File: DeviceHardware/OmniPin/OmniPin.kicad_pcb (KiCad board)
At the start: 2 copper layers, 32 x 38 mm, 52 parts, among them J1 USB_B_Micro, J2 2-1734839-4, J4 Conn_01x02_Pin, Q1 IRLML6402, Q2 IRLML6244, SW1 RST, SW2 BOOT, SW3 POWER, SW4 NEXT, U1 ESP32-C3-MINI-1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

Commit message: update pcb
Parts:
- moved J4 16.7 mm to (106.2, 100.6)
- moved SW2 14.0 mm to (109.5, 100.6)
- moved R5 2.05 mm to (121.5, 98.2), turned to 180 degrees
- moved D6 0.51 mm to (129.0, 97.2)
- moved R13 0.51 mm to (129.0, 98.7)
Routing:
- net GND: track 201.5 -> 214.7 mm, vias 6 -> 9
- net RX: track 6.41 -> 19.3 mm, vias 0 -> 1
- net TX: track 6.06 -> 18.7 mm, vias 0 -> 1
- net Net-(U1-IO9): track 7.65 -> 13.7 mm, vias 0 -> 1
- net +3V3: track 122.2 -> 123.9 mm, vias 7 -> 8
- net IO3: track 33.0 -> 33.8 mm
- net IO1: track 17.4 -> 18.2 mm
- net IO0: track 17.0 -> 17.7 mm
- net D+: track 23.2 -> 22.7 mm
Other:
- board text added: "USR"

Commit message: update pcb
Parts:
- moved C2 4.83 mm to (122.7, 91.1), turned to 180 degrees
- moved R4 4.58 mm to (124.3, 96.2), turned to -90 degrees
- moved C1 1.80 mm to (129.3, 92.6)
- moved Q1 1.78 mm to (126.0, 92.4)
- moved C3 0.13 mm to (122.7, 113.2)
- turned R12 to 90 degrees
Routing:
- net GND: track 214.7 -> 8.92 mm, vias 9 -> 10
- net +3V3: track 123.9 -> 75.9 mm, vias 8 -> 2
- net IO3: track 33.8 -> 28.9 mm
- net VUSB: track 38.8 -> 35.5 mm
- net Net-(U1-EN): track 30.6 -> 31.7 mm
- net BS: track 5.08 -> 4.03 mm
- net Net-(BAT1-Pin_2): track 21.3 -> 20.4 mm
- net Net-(D1-K): track 9.63 -> 8.94 mm
- net PREVGH: track 20.3 -> 20.9 mm
- net D-: track 23.2 -> 22.7 mm
- net Net-(Q1-D): track 9.68 -> 9.58 mm, vias 2 -> 0
- added copper zone on F.Cu, net GND

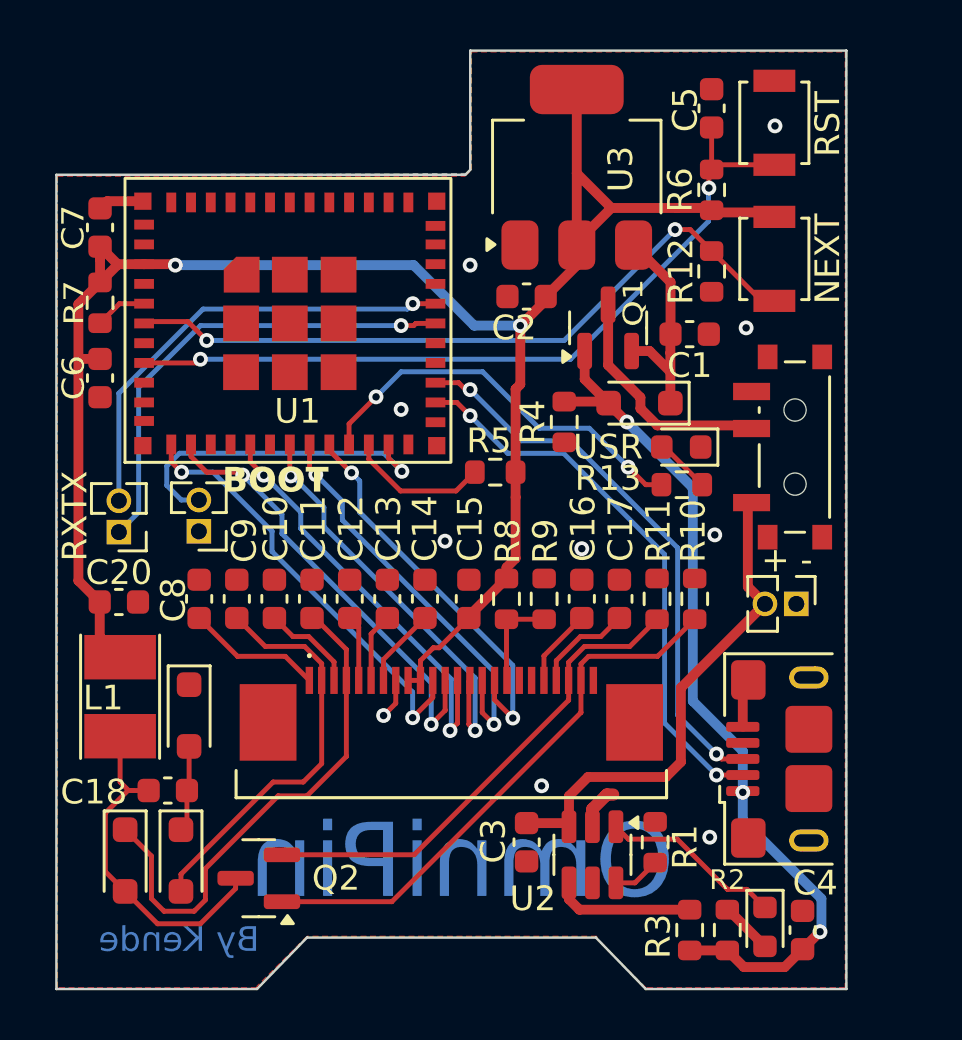
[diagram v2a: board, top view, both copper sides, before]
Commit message: hw panelization
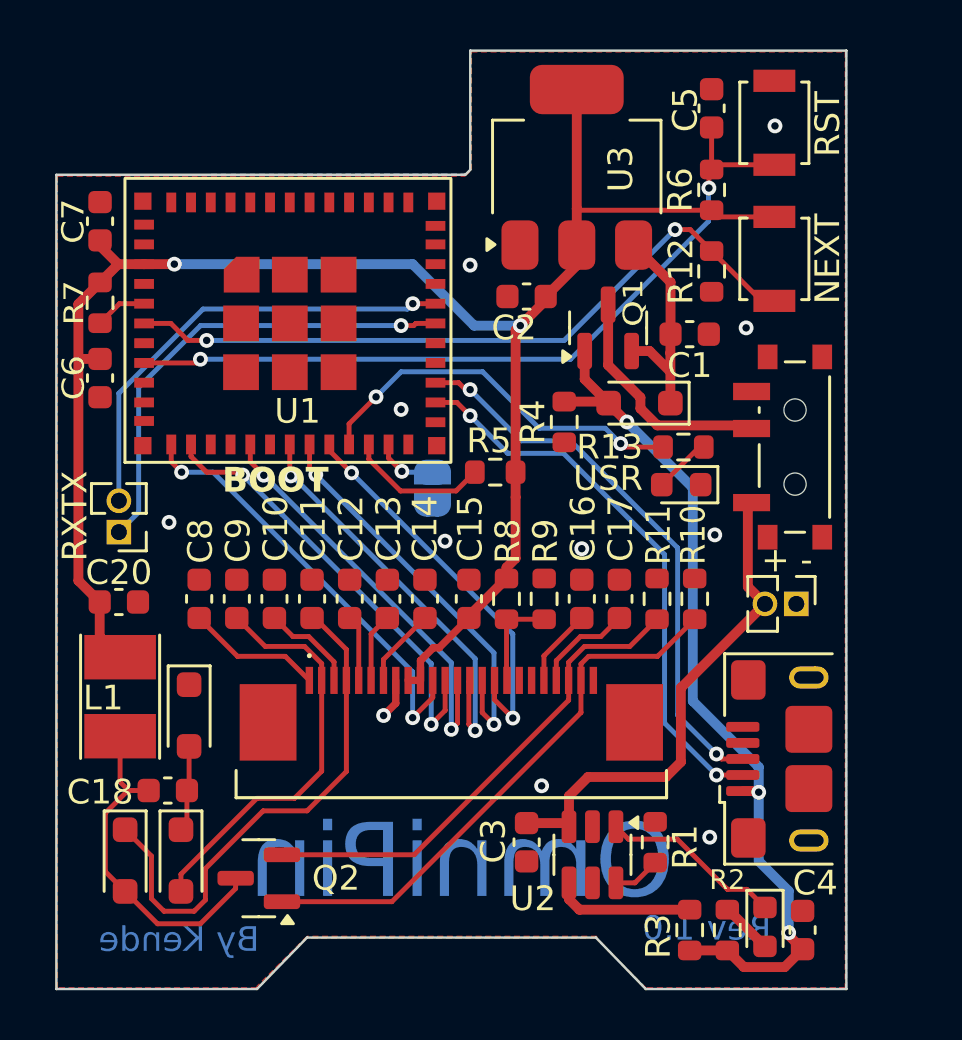
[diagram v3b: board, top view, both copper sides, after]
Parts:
- added T1: Tab, kikit:Tab, F.Cu at (119.4, 117.4)
- added T1: Tab, kikit:Tab, F.Cu at (129.7, 80.9)
- added T1: Tab, kikit:Tab, F.Cu at (136.1, 99.5)
- added T1: Tab, kikit:Tab, F.Cu at (103.4, 99.5)
- SW2: footprint Connector_PinHeader_1.27mm:PinHeader_1x02_P1.27mm_Vertical -> Jumper:SolderJumper-2_P1.3mm_Open_RoundedPad1.0x1.5mm; moved to B.Cu
- moved SW2 9.62 mm to (118.9, 98.8), turned to 90 degrees
- moved R13 1.53 mm to (129.1, 97.2)
- moved D6 1.52 mm to (129.0, 98.7)
- moved C7 0.25 mm to (105.5, 88.0)
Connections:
- J2 pad SH1: Net-(J2-SHIELD-PadSH1) -> GND
- J2 pad SH2: Net-(J2-SHIELD-PadSH1) -> GND
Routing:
- net Net-(U1-IO9): track 13.7 -> 2.57 mm
- net GND: track 8.92 -> 2.91 mm, vias 10 -> 11
- net +3V3: track 75.9 -> 72.1 mm
- net IO7: track 16.3 -> 15.7 mm
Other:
- board text added: "Rev 1.0"

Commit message: update pcb
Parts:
- SW1, SW4: footprint SW_BT:SW_SPST_B3U-1000P -> SW_BT:SW_SPST_B3U-3000P-B
- moved R1 7.60 mm to (133.9, 118.0), turned to 0 degrees
- moved C4 7.52 mm to (126.5, 115.5)
- moved C3 6.12 mm to (128.8, 113.7), turned to 180 degrees
- moved U2 5.92 mm to (130.6, 116.6)
- moved R2 3.66 mm to (133.9, 114.7), turned to 0 degrees
- moved T1 3.18 mm to (103.3, 102.6)
- moved T1 3.18 mm to (136.1, 102.6)
- moved D2 1.55 mm to (133.9, 116.3), turned to 0 degrees
- moved SW1 1.43 mm to (134.2, 84.1)
- moved SW4 1.43 mm to (134.2, 89.6)
- moved R3 1.39 mm to (128.0, 117.2), turned to -90 degrees
- moved J1 0.79 mm to (134.2, 109.0)
- moved BAT1 0.71 mm to (133.6, 102.8)
- moved SW3 0.71 mm to (133.3, 96.5)
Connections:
- J2 pad SH1: GND -> Net-(J2-SHIELD-PadSH1)
- J2 pad SH2: GND -> Net-(J2-SHIELD-PadSH1)
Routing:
- net Net-(D2-K): track 7.39 -> 1.97 mm
- net Net-(U2-V_{CC}): track 5.72 -> 1.75 mm
- net Net-(BAT1-Pin_2): track 20.4 -> 18.8 mm
- net +3V3: track 72.1 -> 73.5 mm
- net IO3: track 28.9 -> 30.3 mm
- net Net-(U1-EN): track 31.7 -> 33.1 mm
- net GND: track 2.91 -> 1.70 mm, vias 11 -> 12
- net VUSB: track 35.5 -> 36.4 mm, vias 3 -> 4
- net D+: track 22.7 -> 21.9 mm
- net D-: track 22.7 -> 21.9 mm
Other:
- board text added: "By: Kende Kurucz Rev: 1.1"
- board text added: "TXRX"
- board text added: "Vesztettél"
- board text removed: "By Kende"
- board text removed: "By: Kende Kurucz Rev: 1.0"
- board text removed: "RXTX"
- board text removed: "Rev 1.0"
